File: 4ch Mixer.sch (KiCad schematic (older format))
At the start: 35 parts, among them J1 JACK_2P, J2 JACK_2P, J3 JACK_2P, J4 JACK_2P, J5 JACK_2P, J6 JACK_2P, U1 TL074, U2 TL072

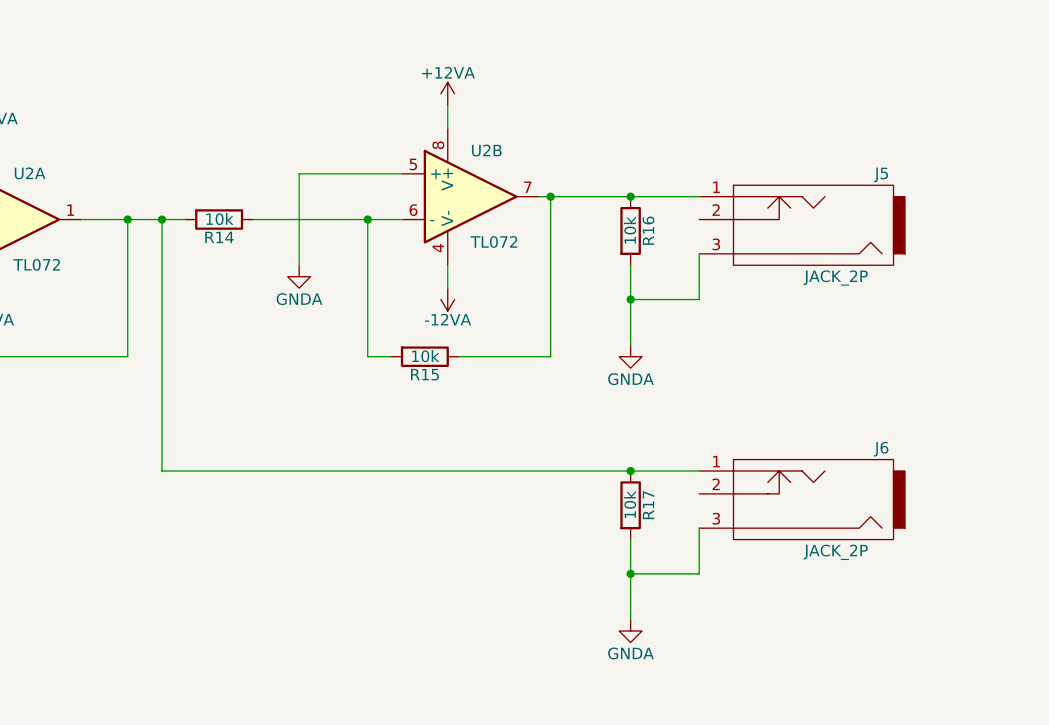
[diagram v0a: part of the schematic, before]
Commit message: Added 100 ohm resistors to outputs.  This is to prevent oscillations when using high capacitance cables.
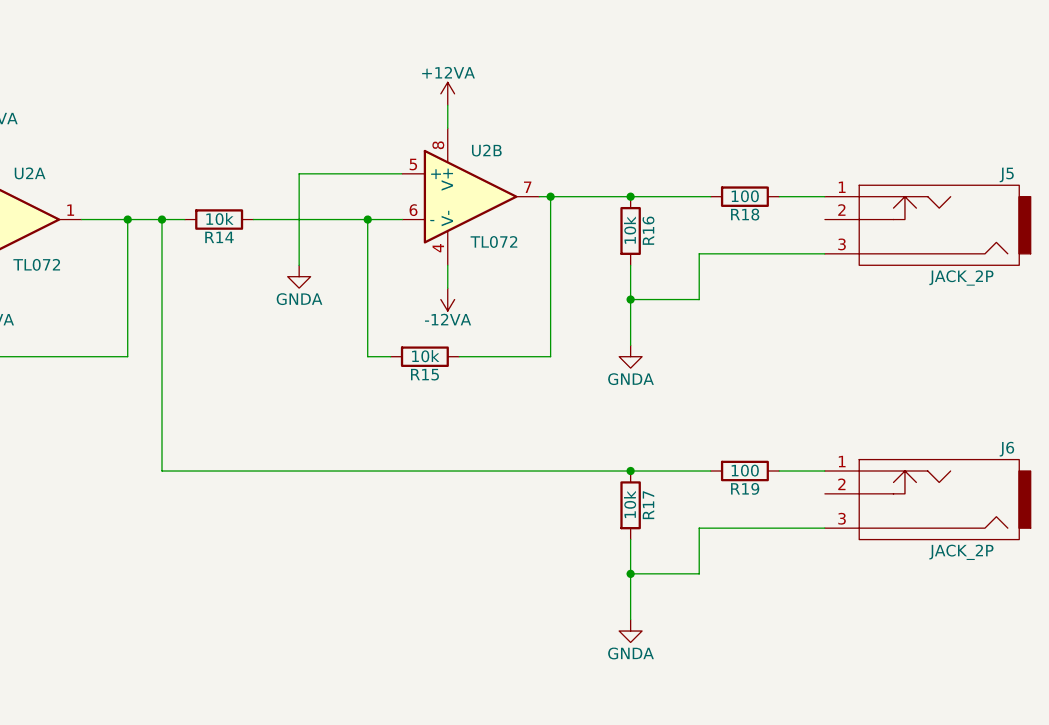
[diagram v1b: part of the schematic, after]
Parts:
- added R18, R19: 100, symbol R
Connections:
- net at R13.1, R14.2, R17.1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: now also R19.2; no longer J6.1
- net at R15.1, R16.1, U2.7: now also R18.2; no longer J5.1
- new net: J5.1, R18.1
- new net: J6.1, R19.1
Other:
- moved on the sheet: J5, J6
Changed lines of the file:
@@
 	7600 4650 7700 4650
-Wire Wire Line
-	8350 3950 9050 3950
 Wire Wire Line
 	7950 3550 7950 3650
@@
 L JACK_2P J5
 U 1 1 58A0E2D1
-P 9500 4050
-F 0 "J5" H 9150 3850 50  0000 C CNN
-F 1 "JACK_2P" H 9350 4300 50  0000 C CNN
-F 2 "Connectors:JACK_ALIM" H 9500 4050 50  0001 C CNN
-F 3 "" H 9500 4050 50  0000 C CNN
-	1    9500 4050
+P 10050 4050
+F 0 "J5" H 9700 3850 50  0000 C CNN
+F 1 "JACK_2P" H 9900 4300 50  0000 C CNN
+F 2 "Connectors:JACK_ALIM" H 10050 4050 50  0001 C CNN
+F 3 "" H 10050 4050 50  0000 C CNN
+	1    10050 4050
 	-1   0    0    1
 $EndComp
@@
 Wire Wire Line
 	8750 4250 8750 4600
-Wire Wire Line
-	8750 4400 9050 4400
-Wire Wire Line
-	9050 4400 9050 4200
-Connection ~ 8750 4400
 $Comp
 L JACK_2P J6
 U 1 1 58A130D4
-P 9500 5250
-F 0 "J6" H 9150 5050 50  0000 C CNN
-F 1 "JACK_2P" H 9350 5500 50  0000 C CNN
-F 2 "Connectors:JACK_ALIM" H 9500 5250 50  0001 C CNN
-F 3 "" H 9500 5250 50  0000 C CNN
-	1    9500 5250
+P 10050 5250
+F 0 "J6" H 9700 5050 50  0000 C CNN
+F 1 "JACK_2P" H 9900 5500 50  0000 C CNN
+F 2 "Connectors:JACK_ALIM" H 10050 5250 50  0001 C CNN
+F 3 "" H 10050 5250 50  0000 C CNN
+	1    10050 5250
 	-1   0    0    1
 $EndComp
@@
 Wire Wire Line
 	8750 5450 8750 5800
-Wire Wire Line
-	6700 5150 9050 5150
-Wire Wire Line
-	9050 5400 9050 5600
-Wire Wire Line
-	9050 5600 8750 5600
-Connection ~ 8750 5600
 Connection ~ 6700 4050
 Connection ~ 8750 5150
@@
 Wire Wire Line
 	7300 3850 7750 3850
+Wire Wire Line
+	6700 5150 9100 5150
+$Comp
+L R R18
+U 1 1 58AD1ABC
+P 9250 3950
+F 0 "R18" V 9330 3950 50  0000 C CNN
+F 1 "100" V 9250 3950 50  0000 C CNN
+F 2 "" V 9180 3950 50  0000 C CNN
+F 3 "" H 9250 3950 50  0000 C CNN
+	1    9250 3950
+	0    1    1    0
+$EndComp
+$Comp
+L R R19
+U 1 1 58AD1BC6
+P 9250 5150
+F 0 "R19" V 9330 5150 50  0000 C CNN
+F 1 "100" V 9250 5150 50  0000 C CNN
+F 2 "" V 9180 5150 50  0000 C CNN
+F 3 "" H 9250 5150 50  0000 C CNN
+	1    9250 5150
+	0    1    1    0
+$EndComp
+Wire Wire Line
+	9400 5150 9600 5150
+Wire Wire Line
+	9600 5400 9050 5400
+Wire Wire Line
+	9050 5400 9050 5600
+Wire Wire Line
+	9050 5600 8750 5600
+Connection ~ 8750 5600
+Wire Wire Line
+	9600 3950 9400 3950
+Wire Wire Line
+	9100 3950 8350 3950
+Wire Wire Line
+	9600 4200 9050 4200
+Wire Wire Line
+	9050 4200 9050 4400
+Wire Wire Line
+	9050 4400 8750 4400
+Connection ~ 8750 4400
 $EndSCHEMATC

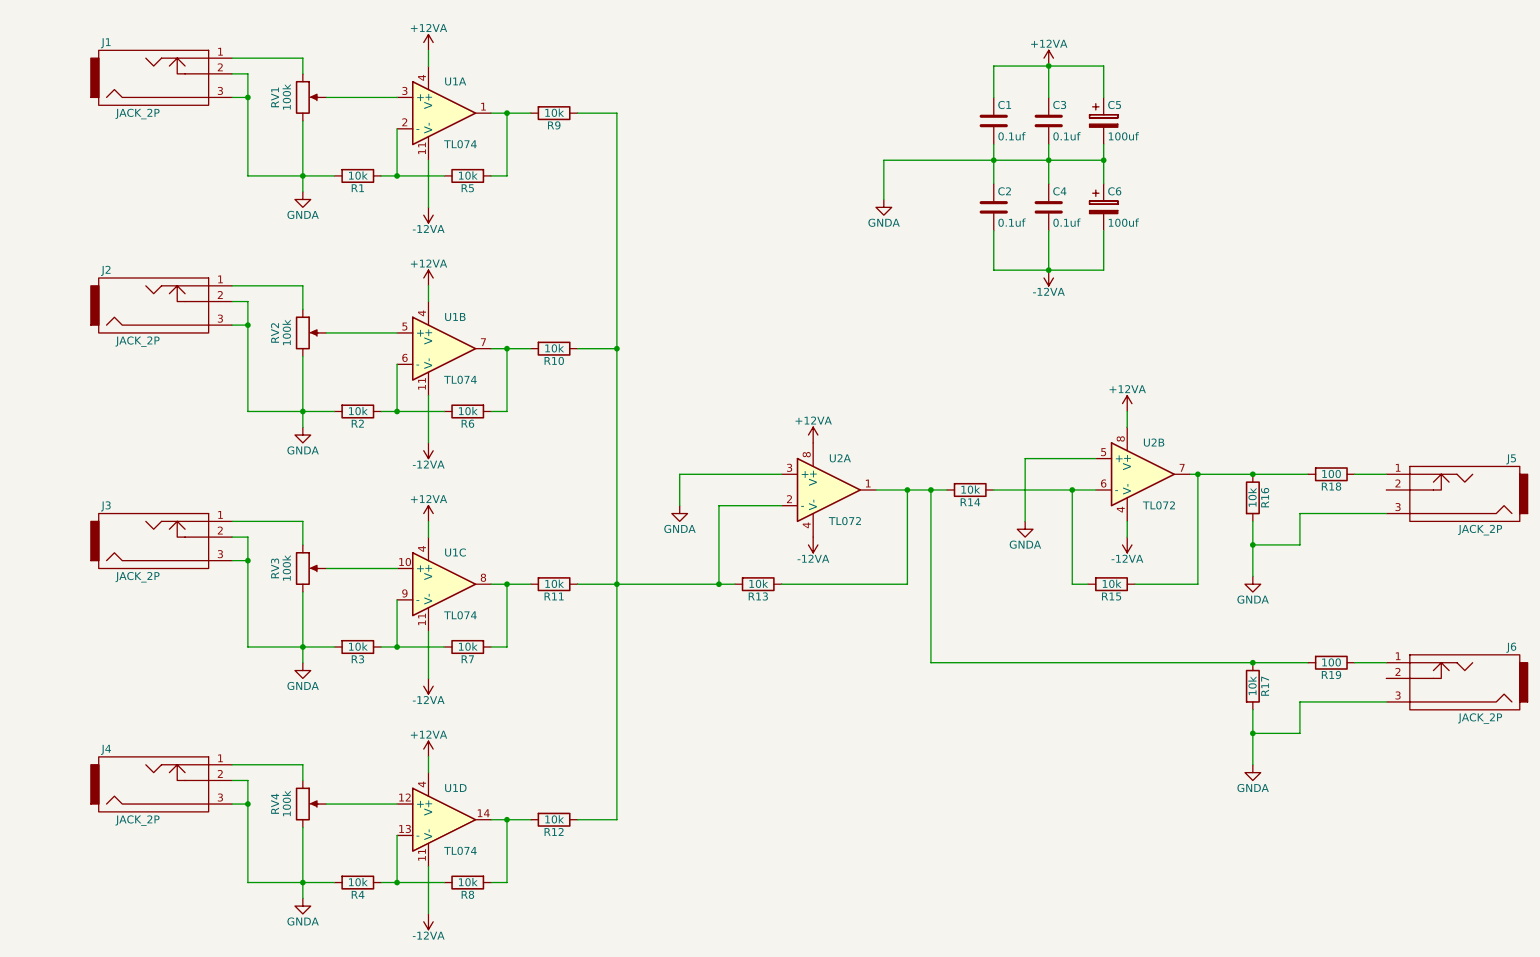
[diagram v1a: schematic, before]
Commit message: Added PTC fuses and protection diodes to schematic.
Associated footprints.
Started a PCB layout, need to update some footprints.
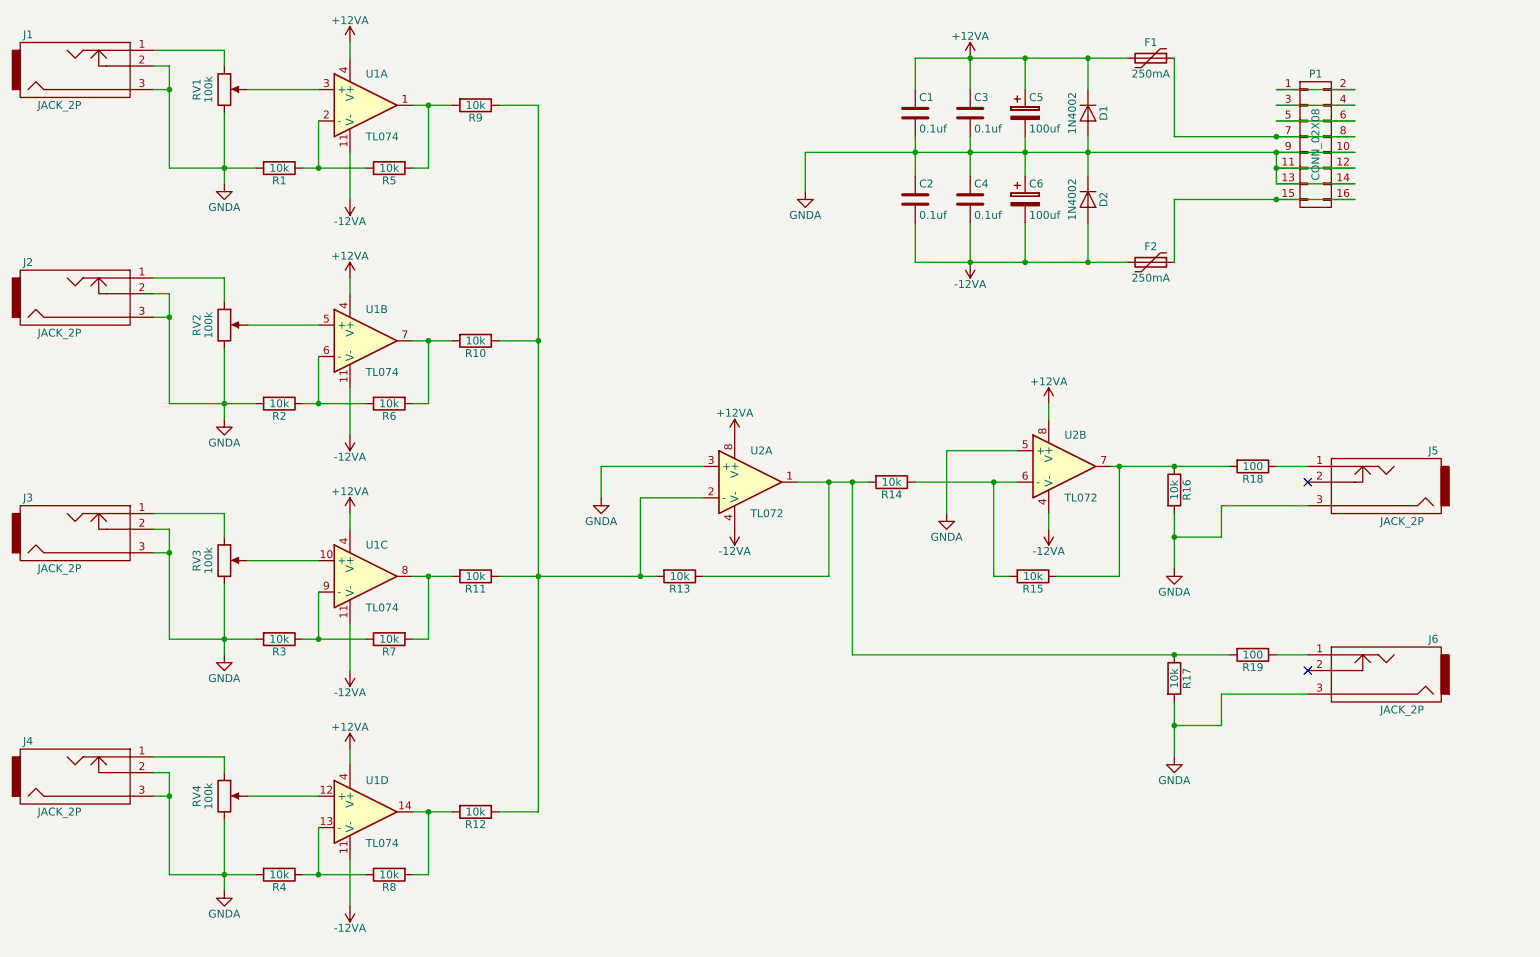
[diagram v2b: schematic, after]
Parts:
- added D1, D2: 1N4002, Diodes_THT:D_DO-15_P12.70mm_Horizontal, symbol D
- added F1, F2: 250mA, Capacitors_THT:C_Disc_D5.0mm_W2.5mm_P5.00mm, symbol Polyfuse
- added P1: CONN_02X08, Pin_Headers:Pin_Header_Straight_2x08_Pitch2.54mm, symbol CONN_02X08
- R18, R19: footprint (none) -> Resistors_THT:R_Axial_DIN0309_L9.0mm_D3.2mm_P12.70mm_Horizontal
- RV1, RV2, RV3, RV4: footprint Potentiometers:Potentiometer_Alps-RK16-single_largePads -> Potentiometers:Potentiometer_Alps_RK09L_Sleve_Single_Horizontal
- U1: footprint Housings_DIP:DIP-8_W7.62mm_Socket -> Housings_DIP:DIP-14_W7.62mm_Socket
- U2: footprint Housings_DIP:DIP-14_W7.62mm_Socket -> Housings_DIP:DIP-8_W7.62mm_Socket
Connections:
- net +12VA: now also D1.1 (K), F1.2
- net -12VA: now also D2.2 (A), F2.2
- net GNDA: now also D1.2 (A), D2.1 (K), P1.10 (P10), P1.11 (P11), P1.12 (P12), P1.13 (P13), P1.14 (P14), P1.9 (P9)
- new net: P1.1 (P1), P1.2 (P2)
- new net: F2.1, P1.15 (P15), P1.16 (P16)
- new net: P1.3 (P3), P1.4 (P4)
- new net: P1.5 (P5), P1.6 (P6)
- new net: F1.1, P1.7 (P7), P1.8 (P8)
- no-connect marks 0 -> 2
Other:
- moved on the sheet: C1, C2, C3, C4, C5, C6, J1, J2, J3, J4, J5, J6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

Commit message: Continued work on PCB and Schematic
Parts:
- removed J1, J2, J3, J4, J5, J6: JACK_2P, Connectors:JACK_ALIM, symbol JACK_2P
- added J1, J2, J3, J4, J5, J6: 3.5mm_Mono_Jack_With_Switch, _NTSFootprints:3.5mm_Mono_Vertical_QuingPu_WQP-PJ301M-12, symbol 3.5mm_Mono_Jack_With_Switch
- C1, C2, C3, C4: footprint Capacitors_THT:C_Rect_L11.0mm_W3.4mm_P10.00mm_MKT -> Capacitors_THT:C_Axial_L5.1mm_D3.1mm_P10.00mm_Horizontal
- C5, C6: footprint Capacitors_THT:CP_Radial_D10.0mm_P7.50mm -> Capacitors_THT:CP_Radial_D8.0mm_P5.00mm
- D1, D2: footprint Diodes_THT:D_DO-15_P12.70mm_Horizontal -> Diodes_THT:D_DO-35_SOD27_P2.54mm_Vertical_AnodeUp
- R1, R10, R11, R12, R13, R14, R15, R16, R17, R18, R19, R2, R3, R4, R5, R6, R7, R8, R9: footprint Resistors_THT:R_Axial_DIN0309_L9.0mm_D3.2mm_P12.70mm_Horizontal -> Resistors_THT:R_Axial_DIN0207_L6.3mm_D2.5mm_P2.54mm_Vertical
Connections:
- net GNDA: now also J1.1, J1.2, J2.1, J2.2, J3.1, J3.2, J4.1, J4.2, J5.1, J6.1
- net at RV1.1: now also J1.3
- net at RV2.1: now also J2.3
- net at RV3.1: now also J3.3
- net at RV4.1: now also J4.3
- net at R18.1: now also J5.3
- net at R19.1: now also J6.3
